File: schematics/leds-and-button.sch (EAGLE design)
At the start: 10 parts

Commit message: Reworked the boards
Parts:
- renumbered JP4 to BTN, LED_12V to 12V, LED_3.3V to 3.3V, LED_5V to 5V, LED_9V to 9V, LED_ADJV to ADJV
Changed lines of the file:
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@@
 <?xml version="1.0" encoding="utf-8"?>
 <!DOCTYPE eagle SYSTEM "eagle.dtd">
-<eagle version="6.1">
+<eagle version="7.4.0">
 <drawing>
 <settings>
@@
 </classes>
 <parts>
-<part name="LED_3.3V" library="SparkFun" deviceset="LED" device="-3MM-NO_SILK"/>
-<part name="LED_5V" library="SparkFun" deviceset="LED" device="-3MM-NO_SILK"/>
-<part name="LED_9V" library="SparkFun" deviceset="LED" device="-3MM-NO_SILK"/>
-<part name="LED_12V" library="SparkFun" deviceset="LED" device="-3MM-NO_SILK"/>
-<part name="LED_ADJV" library="SparkFun" deviceset="LED" device="-3MM-NO_SILK"/>
+<part name="3.3V" library="SparkFun" deviceset="LED" device="-3MM-NO_SILK"/>
+<part name="5V" library="SparkFun" deviceset="LED" device="-3MM-NO_SILK"/>
+<part name="9V" library="SparkFun" deviceset="LED" device="-3MM-NO_SILK"/>
+<part name="12V" library="SparkFun" deviceset="LED" device="-3MM-NO_SILK"/>
+<part name="ADJV" library="SparkFun" deviceset="LED" device="-3MM-NO_SILK"/>
 <part name="JP3" library="SparkFun" deviceset="M08" device="1X08"/>
 <part name="RN1" library="resistor-net" deviceset="RNX5" device="" value="330"/>
 <part name="JP1" library="SparkFun" deviceset="STAND-OFF" device=""/>
 <part name="JP2" library="SparkFun" deviceset="STAND-OFF" device=""/>
-<part name="JP4" library="SparkFun" deviceset="M02" device="PTH"/>
+<part name="BTN" library="SparkFun" deviceset="M02" device="PTH"/>
 </parts>
 <sheets>
@@
 </plain>
 <instances>
-<instance part="LED_3.3V" gate="G$1" x="10.16" y="25.4"/>
-<instance part="LED_5V" gate="G$1" x="17.78" y="25.4"/>
-<instance part="LED_9V" gate="G$1" x="25.4" y="25.4"/>
-<instance part="LED_12V" gate="G$1" x="33.02" y="25.4"/>
-<instance part="LED_ADJV" gate="G$1" x="40.64" y="25.4"/>
+<instance part="3.3V" gate="G$1" x="10.16" y="25.4"/>
+<instance part="5V" gate="G$1" x="17.78" y="25.4"/>
+<instance part="9V" gate="G$1" x="25.4" y="25.4"/>
+<instance part="12V" gate="G$1" x="33.02" y="25.4"/>
+<instance part="ADJV" gate="G$1" x="40.64" y="25.4"/>
 <instance part="JP3" gate="G$1" x="22.86" y="45.72" rot="R270"/>
 <instance part="RN1" gate="_" x="45.72" y="12.7" rot="R270"/>
@@
 <instance part="JP1" gate="G$1" x="2.54" y="15.24"/>
 <instance part="JP2" gate="G$1" x="2.54" y="10.16"/>
-<instance part="JP4" gate="G$1" x="7.62" y="35.56"/>
+<instance part="BTN" gate="G$1" x="7.62" y="35.56"/>
 </instances>
 <busses>
@@
 <wire x1="20.32" y1="40.64" x2="20.32" y2="30.48" width="0.1524" layer="91"/>
 <wire x1="20.32" y1="30.48" x2="10.16" y2="30.48" width="0.1524" layer="91"/>
-<pinref part="LED_3.3V" gate="G$1" pin="A"/>
+<pinref part="3.3V" gate="G$1" pin="A"/>
 </segment>
 </net>
@@
 <wire x1="22.86" y1="40.64" x2="22.86" y2="27.94" width="0.1524" layer="91"/>
 <wire x1="22.86" y1="27.94" x2="17.78" y2="27.94" width="0.1524" layer="91"/>
-<pinref part="LED_5V" gate="G$1" pin="A"/>
+<pinref part="5V" gate="G$1" pin="A"/>
 </segment>
 </net>
@@
 <pinref part="JP3" gate="G$1" pin="5"/>
 <wire x1="25.4" y1="40.64" x2="25.4" y2="27.94" width="0.1524" layer="91"/>
-<pinref part="LED_9V" gate="G$1" pin="A"/>
+<pinref part="9V" gate="G$1" pin="A"/>
 </segment>
 </net>
@@
 <wire x1="27.94" y1="40.64" x2="27.94" y2="27.94" width="0.1524" layer="91"/>
 <wire x1="27.94" y1="27.94" x2="33.02" y2="27.94" width="0.1524" layer="91"/>
-<pinref part="LED_12V" gate="G$1" pin="A"/>
+<pinref part="12V" gate="G$1" pin="A"/>
 </segment>
 </net>
@@
 <wire x1="30.48" y1="40.64" x2="30.48" y2="30.48" width="0.1524" layer="91"/>
 <wire x1="30.48" y1="30.48" x2="40.64" y2="30.48" width="0.1524" layer="91"/>
-<pinref part="LED_ADJV" gate="G$1" pin="A"/>
+<pinref part="ADJV" gate="G$1" pin="A"/>
 </segment>
 </net>
@@
 <net name="N$2" class="0">
 <segment>
-<pinref part="LED_3.3V" gate="G$1" pin="C"/>
+<pinref part="3.3V" gate="G$1" pin="C"/>
 <pinref part="RN1" gate="-5" pin="1"/>
 <wire x1="10.16" y1="20.32" x2="10.16" y2="17.78" width="0.1524" layer="91"/>
@@
 <net name="N$3" class="0">
 <segment>
-<pinref part="LED_5V" gate="G$1" pin="C"/>
+<pinref part="5V" gate="G$1" pin="C"/>
 <pinref part="RN1" gate="-4" pin="1"/>
 <wire x1="17.78" y1="20.32" x2="17.78" y2="17.78" width="0.1524" layer="91"/>
@@
 <segment>
 <pinref part="RN1" gate="-3" pin="1"/>
-<pinref part="LED_9V" gate="G$1" pin="C"/>
+<pinref part="9V" gate="G$1" pin="C"/>
 <wire x1="25.4" y1="17.78" x2="25.4" y2="20.32" width="0.1524" layer="91"/>
 </segment>
@@
 <segment>
 <pinref part="RN1" gate="-2" pin="1"/>
-<pinref part="LED_12V" gate="G$1" pin="C"/>
+<pinref part="12V" gate="G$1" pin="C"/>
 <wire x1="33.02" y1="17.78" x2="33.02" y2="20.32" width="0.1524" layer="91"/>
 </segment>
@@
 <segment>
 <pinref part="RN1" gate="-1" pin="1"/>
-<pinref part="LED_ADJV" gate="G$1" pin="C"/>
+<pinref part="ADJV" gate="G$1" pin="C"/>
 <wire x1="40.64" y1="17.78" x2="40.64" y2="20.32" width="0.1524" layer="91"/>
 </segment>
@@
 <segment>
 <pinref part="JP3" gate="G$1" pin="1"/>
-<pinref part="JP4" gate="G$1" pin="2"/>
+<pinref part="BTN" gate="G$1" pin="2"/>
 <wire x1="15.24" y1="38.1" x2="15.24" y2="40.64" width="0.1524" layer="91"/>
 </segment>
@@
 <net name="N$12" class="0">
 <segment>
-<pinref part="JP4" gate="G$1" pin="1"/>
+<pinref part="BTN" gate="G$1" pin="1"/>
 <wire x1="15.24" y1="35.56" x2="17.78" y2="35.56" width="0.1524" layer="91"/>
 <wire x1="17.78" y1="35.56" x2="17.78" y2="38.1" width="0.1524" layer="91"/>

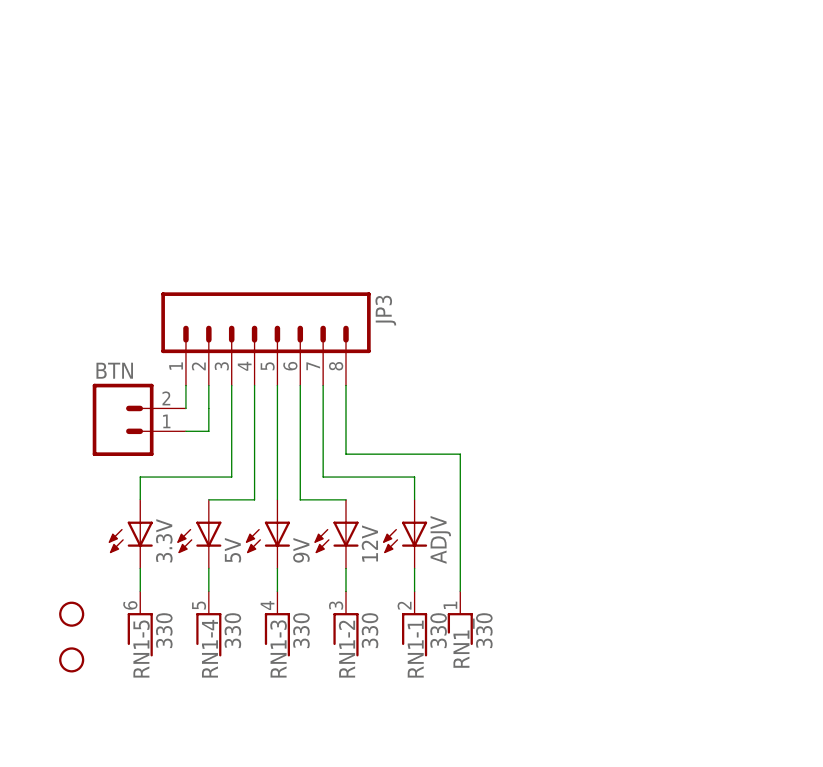
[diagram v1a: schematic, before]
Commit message: Moved the shift register to the top board since I have more room there and on the bottom board and I get to free up some pins on the jumper
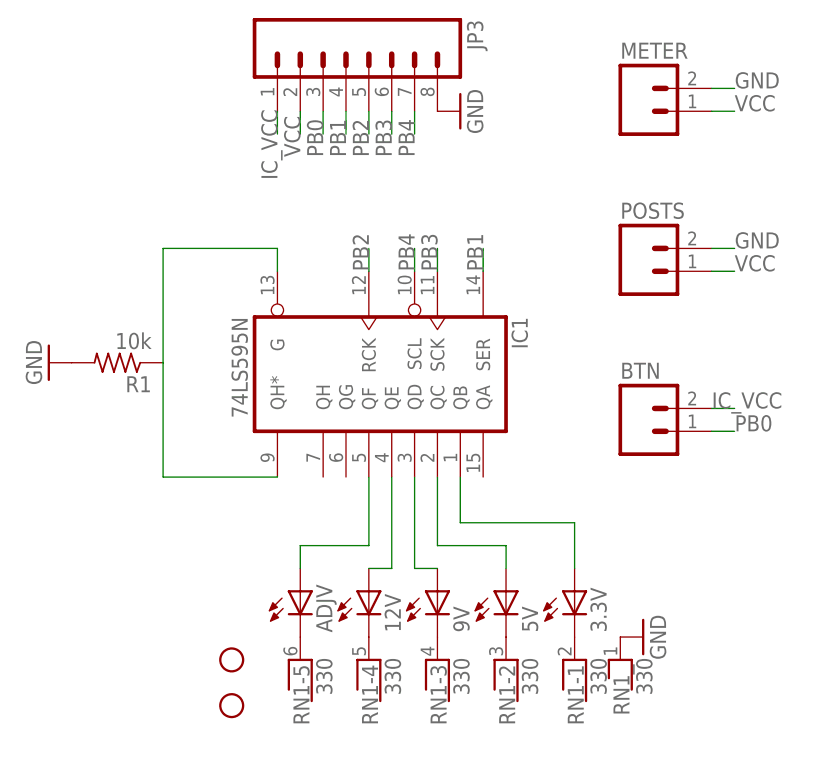
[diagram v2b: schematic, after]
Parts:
- added IC1: 74LS595N, 74xx-us:74LS595N
- added METER, POSTS: (no value), SparkFun:M02PTH
- added R1: 10k, resistor:R-US_0204/2V
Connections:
- net N$11 renamed IC_VCC
- removed net N$1: JP3.8, RN1_.1
- removed net N$12: BTN.1, JP3.2
- new net GND: JP3.8, METER.2, POSTS.2, R1.2, RN1_.1
- new net N$11: IC1A.G, IC1A.QH*, R1.1
- new net PB0: BTN.1, JP3.3
- new net PB1: IC1A.SER, JP3.4
- new net PB2: IC1A.RCK, JP3.5
- new net PB3: IC1A.SCK, JP3.6
- new net PB4: IC1A.SCL, JP3.7
- new net VCC: JP3.2, METER.1, POSTS.1
- net N$10: now also 3.3V.C; no longer ADJV.C
- net N$13: now also 3.3V.A, IC1A.QB; no longer ADJV.A, JP3.7
- net N$2: now also ADJV.C; no longer 3.3V.C
- net N$3: now also 12V.C; no longer 5V.C
- net N$4: now also ADJV.A, IC1A.QF; no longer 3.3V.A, JP3.3
- net N$5: now also 12V.A, IC1A.QE; no longer 5V.A, JP3.4
- net N$6: now also IC1A.QD; no longer JP3.5
- net N$7: now also 5V.A, IC1A.QC; no longer 12V.A, JP3.6
- net N$9: now also 5V.C; no longer 12V.C
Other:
- moved on the sheet: 12V, 3.3V, 5V, 9V, ADJV, BTN, JP3, RN1-1, RN1-2, RN1-3, RN1-4, RN1-5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

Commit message: Updated the schematics
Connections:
- net IC_VCC: now also IC1A.SCL
- net PB2: now also IC1A.SCK; no longer IC1A.RCK
- net PB3: now also IC1A.RCK; no longer IC1A.SCK
- net PB4: no longer IC1A.SCL
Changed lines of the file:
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@@
 <label x="73.66" y="38.1" size="1.778" layer="95"/>
+</segment>
+<segment>
+<pinref part="IC1" gate="A" pin="SCL"/>
+<wire x1="40.64" y1="53.34" x2="40.64" y2="55.88" width="0.1524" layer="91"/>
+<label x="40.64" y="53.34" size="1.778" layer="95" rot="R90"/>
 </segment>
 </net>
@@
 <net name="PB3" class="0">
 <segment>
-<pinref part="IC1" gate="A" pin="SCK"/>
-<wire x1="43.18" y1="53.34" x2="43.18" y2="55.88" width="0.1524" layer="91"/>
-<label x="43.18" y="53.34" size="1.778" layer="95" rot="R90"/>
-</segment>
-<segment>
 <pinref part="JP3" gate="G$1" pin="6"/>
 <wire x1="38.1" y1="71.12" x2="38.1" y2="68.58" width="0.1524" layer="91"/>
 <label x="38.1" y="66.04" size="1.778" layer="95" rot="R90"/>
 </segment>
+<segment>
+<pinref part="IC1" gate="A" pin="RCK"/>
+<wire x1="35.56" y1="53.34" x2="35.56" y2="55.88" width="0.1524" layer="91"/>
+<label x="35.56" y="53.34" size="1.778" layer="95" rot="R90"/>
+</segment>
 </net>
 <net name="PB4" class="0">
-<segment>
-<pinref part="IC1" gate="A" pin="SCL"/>
-<wire x1="40.64" y1="53.34" x2="40.64" y2="55.88" width="0.1524" layer="91"/>
-<label x="40.64" y="53.34" size="1.778" layer="95" rot="R90"/>
-</segment>
 <segment>
 <pinref part="JP3" gate="G$1" pin="7"/>
@@
 <net name="PB2" class="0">
 <segment>
-<pinref part="IC1" gate="A" pin="RCK"/>
-<wire x1="35.56" y1="53.34" x2="35.56" y2="55.88" width="0.1524" layer="91"/>
-<label x="35.56" y="53.34" size="1.778" layer="95" rot="R90"/>
-</segment>
-<segment>
 <pinref part="JP3" gate="G$1" pin="5"/>
 <wire x1="35.56" y1="71.12" x2="35.56" y2="68.58" width="0.1524" layer="91"/>
 <label x="35.56" y="66.04" size="1.778" layer="95" rot="R90"/>
 </segment>
+<segment>
+<pinref part="IC1" gate="A" pin="SCK"/>
+<wire x1="43.18" y1="53.34" x2="43.18" y2="55.88" width="0.1524" layer="91"/>
+<label x="43.18" y="53.34" size="1.778" layer="95" rot="R90"/>
+</segment>
 </net>

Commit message: Played around with the board for the leds
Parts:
- removed JP1: STAND-OFF, SparkFun:STAND-OFF
- 12V, 3.3V, 5V, 9V, ADJV: device SparkFun:LED-3MM-NO_SILK -> SparkFun-LED:LED3MM
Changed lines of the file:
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@@
 <layer number="54" name="bGND_GNDA" color="1" fill="9" visible="no" active="no"/>
 <layer number="56" name="wert" color="7" fill="1" visible="no" active="no"/>
+<layer number="57" name="tCAD" color="7" fill="1" visible="no" active="no"/>
+<layer number="59" name="tCarbon" color="7" fill="1" visible="no" active="no"/>
+<layer number="60" name="bCarbon" color="7" fill="1" visible="no" active="no"/>
+<layer number="90" name="Modules" color="5" fill="1" visible="no" active="no"/>
 <layer number="91" name="Nets" color="2" fill="1" visible="yes" active="yes"/>
 <layer number="92" name="Busses" color="1" fill="1" visible="yes" active="yes"/>
@@
 <layer number="111" name="LPC17xx" color="7" fill="1" visible="yes" active="yes"/>
 <layer number="112" name="tSilk" color="7" fill="1" visible="yes" active="yes"/>
+<layer number="113" name="IDFDebug" color="4" fill="1" visible="yes" active="yes"/>
 <layer number="116" name="Patch_BOT" color="9" fill="4" visible="yes" active="yes"/>
+<layer number="118" name="Rect_Pads" color="7" fill="1" visible="yes" active="yes"/>
 <layer number="121" name="_tsilk" color="7" fill="1" visible="no" active="yes"/>
 <layer number="122" name="_bsilk" color="7" fill="1" visible="no" active="yes"/>
@@
 <layer number="127" name="_tValues" color="7" fill="1" visible="yes" active="yes"/>
 <layer number="128" name="_bValues" color="7" fill="1" visible="yes" active="yes"/>
+<layer number="129" name="Mask" color="7" fill="1" visible="yes" active="yes"/>
 <layer number="131" name="tAdjust" color="7" fill="1" visible="no" active="yes"/>
 <layer number="132" name="bAdjust" color="7" fill="1" visible="no" active="yes"/>
 <layer number="144" name="Drill_legend" color="7" fill="1" visible="no" active="yes"/>
+<layer number="150" name="Notes" color="7" fill="1" visible="yes" active="yes"/>
 <layer number="151" name="HeatSink" color="7" fill="1" visible="yes" active="yes"/>
 <layer number="152" name="_bDocu" color="7" fill="1" visible="yes" active="yes"/>
+<layer number="153" name="FabDoc1" color="7" fill="1" visible="yes" active="yes"/>
+<layer number="154" name="FabDoc2" color="7" fill="1" visible="yes" active="yes"/>
+<layer number="155" name="FabDoc3" color="7" fill="1" visible="yes" active="yes"/>
 <layer number="199" name="Contour" color="7" fill="1" visible="yes" active="yes"/>
 <layer number="200" name="200bmp" color="1" fill="10" visible="no" active="no"/>
@@
 <layer number="223" name="223bmp" color="24" fill="1" visible="no" active="no"/>
 <layer number="224" name="224bmp" color="25" fill="1" visible="no" active="no"/>
+<layer number="225" name="225bmp" color="7" fill="1" visible="yes" active="yes"/>
+<layer number="226" name="226bmp" color="7" fill="1" visible="yes" active="yes"/>
+<layer number="227" name="227bmp" color="7" fill="1" visible="yes" active="yes"/>
+<layer number="228" name="228bmp" color="7" fill="1" visible="yes" active="yes"/>
+<layer number="229" name="229bmp" color="7" fill="1" visible="yes" active="yes"/>
+<layer number="230" name="230bmp" color="7" fill="1" visible="yes" active="yes"/>
+<layer number="231" name="231bmp" color="7" fill="1" visible="yes" active="yes"/>
 <layer number="248" name="Housing" color="7" fill="1" visible="yes" active="yes"/>
 <layer number="249" name="Edge" color="7" fill="1" visible="yes" active="yes"/>
@@
 <layer number="251" name="SMDround" color="7" fill="1" visible="no" active="no"/>
 <layer number="254" name="cooling" color="7" fill="1" visible="yes" active="yes"/>
+<layer number="255" name="routoute" color="7" fill="1" visible="yes" active="yes"/>
 </layers>
 <schematic>
@@
 </classes>
 <parts>
-<part name="ADJV" library="SparkFun" deviceset="LED" device="-3MM-NO_SILK"/>
-<part name="12V" library="SparkFun" deviceset="LED" device="-3MM-NO_SILK"/>
-<part name="9V" library="SparkFun" deviceset="LED" device="-3MM-NO_SILK"/>
-<part name="5V" library="SparkFun" deviceset="LED" device="-3MM-NO_SILK"/>
-<part name="3.3V" library="SparkFun" deviceset="LED" device="-3MM-NO_SILK"/>
 <part name="JP3" library="SparkFun" deviceset="M08" device="1X08"/>
 <part name="RN1" library="resistor-net" deviceset="RNX5" device="" value="330"/>
-<part name="JP1" library="SparkFun" deviceset="STAND-OFF" device=""/>
 <part name="JP2" library="SparkFun" deviceset="STAND-OFF" device=""/>
 <part name="BTN" library="SparkFun" deviceset="M02" device="PTH"/>
@@
 <part name="POSTS" library="SparkFun" deviceset="M02" device="PTH"/>
 <part name="METER" library="SparkFun" deviceset="M02" device="PTH"/>
+<part name="ADJV" library="SparkFun-LED" deviceset="LED" device="3MM"/>
+<part name="12V" library="SparkFun-LED" deviceset="LED" device="3MM"/>
+<part name="9V" library="SparkFun-LED" deviceset="LED" device="3MM"/>
+<part name="5V" library="SparkFun-LED" deviceset="LED" device="3MM"/>
+<part name="3.3V" library="SparkFun-LED" deviceset="LED" device="3MM"/>
 </parts>
 <sheets>
@@
 </plain>
 <instances>
-<instance part="ADJV" gate="G$1" x="27.94" y="17.78"/>
-<instance part="12V" gate="G$1" x="35.56" y="17.78"/>
-<instance part="9V" gate="G$1" x="43.18" y="17.78"/>
-<instance part="5V" gate="G$1" x="50.8" y="17.78"/>
-<instance part="3.3V" gate="G$1" x="58.42" y="17.78"/>
 <instance part="JP3" gate="G$1" x="33.02" y="76.2" rot="R270"/>
 <instance part="RN1" gate="_" x="63.5" y="7.62" rot="R270"/>
@@
 <instance part="RN1" gate="-4" x="35.56" y="10.16" rot="R270"/>
 <instance part="RN1" gate="-5" x="27.94" y="10.16" rot="R270"/>
-<instance part="JP1" gate="G$1" x="20.32" y="10.16"/>
 <instance part="JP2" gate="G$1" x="20.32" y="5.08"/>
 <instance part="BTN" gate="G$1" x="66.04" y="35.56"/>
@@
 <instance part="POSTS" gate="G$1" x="66.04" y="53.34"/>
 <instance part="METER" gate="G$1" x="66.04" y="71.12"/>
+<instance part="ADJV" gate="G$1" x="27.94" y="17.78"/>
+<instance part="12V" gate="G$1" x="35.56" y="17.78"/>
+<instance part="9V" gate="G$1" x="43.18" y="17.78"/>
+<instance part="5V" gate="G$1" x="50.8" y="17.78"/>
+<instance part="3.3V" gate="G$1" x="58.42" y="17.78"/>
 </instances>
 <busses>
@@
 <net name="N$4" class="0">
 <segment>
-<pinref part="ADJV" gate="G$1" pin="A"/>
 <wire x1="27.94" y1="22.86" x2="27.94" y2="20.32" width="0.1524" layer="91"/>
 <wire x1="35.56" y1="22.86" x2="27.94" y2="22.86" width="0.1524" layer="91"/>
 <pinref part="IC1" gate="A" pin="QF"/>
 <wire x1="35.56" y1="22.86" x2="35.56" y2="30.48" width="0.1524" layer="91"/>
+<pinref part="ADJV" gate="G$1" pin="A"/>
 </segment>
 </net>
 <net name="N$5" class="0">
 <segment>
-<pinref part="12V" gate="G$1" pin="A"/>
 <wire x1="35.56" y1="20.32" x2="38.1" y2="20.32" width="0.1524" layer="91"/>
 <pinref part="IC1" gate="A" pin="QE"/>
 <wire x1="38.1" y1="20.32" x2="38.1" y2="30.48" width="0.1524" layer="91"/>
+<pinref part="12V" gate="G$1" pin="A"/>
 </segment>
 </net>
@@
 <segment>
 <wire x1="50.8" y1="22.86" x2="50.8" y2="20.32" width="0.1524" layer="91"/>
-<pinref part="5V" gate="G$1" pin="A"/>
 <wire x1="50.8" y1="22.86" x2="43.18" y2="22.86" width="0.1524" layer="91"/>
 <pinref part="IC1" gate="A" pin="QC"/>
 <wire x1="43.18" y1="22.86" x2="43.18" y2="30.48" width="0.1524" layer="91"/>
+<pinref part="5V" gate="G$1" pin="A"/>
 </segment>
 </net>
@@
 <segment>
 <wire x1="58.42" y1="25.4" x2="58.42" y2="20.32" width="0.1524" layer="91"/>
-<pinref part="3.3V" gate="G$1" pin="A"/>
 <wire x1="58.42" y1="25.4" x2="45.72" y2="25.4" width="0.1524" layer="91"/>
 <pinref part="IC1" gate="A" pin="QB"/>
 <wire x1="45.72" y1="30.48" x2="45.72" y2="25.4" width="0.1524" layer="91"/>
-</segment>
-</net>
-<net name="N$2" class="0">
-<segment>
-<pinref part="ADJV" gate="G$1" pin="C"/>
-<pinref part="RN1" gate="-5" pin="1"/>
-</segment>
-</net>
-<net name="N$3" class="0">
-<segment>
-<pinref part="12V" gate="G$1" pin="C"/>
-<pinref part="RN1" gate="-4" pin="1"/>
-</segment>
-</net>
-<net name="N$8" class="0">
-<segment>
-<pinref part="RN1" gate="-3" pin="1"/>
-<pinref part="9V" gate="G$1" pin="C"/>
-</segment>
-</net>
-<net name="N$9" class="0">
-<segment>
-<pinref part="RN1" gate="-2" pin="1"/>
-<pinref part="5V" gate="G$1" pin="C"/>
-</segment>
-</net>
-<net name="N$10" class="0">
-<segment>
-<pinref part="RN1" gate="-1" pin="1"/>
-<pinref part="3.3V" gate="G$1" pin="C"/>
+<pinref part="3.3V" gate="G$1" pin="A"/>
 </segment>
 </net>
@@
 <net name="N$6" class="0">
 <segment>
-<pinref part="9V" gate="G$1" pin="A"/>
 <wire x1="43.18" y1="20.32" x2="40.64" y2="20.32" width="0.1524" layer="91"/>
 <pinref part="IC1" gate="A" pin="QD"/>
 <wire x1="40.64" y1="20.32" x2="40.64" y2="30.48" width="0.1524" layer="91"/>
+<pinref part="9V" gate="G$1" pin="A"/>
 </segment>
 </net>
@@
 </segment>
 </net>
+<net name="N$1" class="0">
+<segment>
+<pinref part="RN1" gate="-5" pin="1"/>
+<pinref part="ADJV" gate="G$1" pin="C"/>
+</segment>
+</net>
+<net name="N$2" class="0">
+<segment>
+<pinref part="RN1" gate="-4" pin="1"/>
+<pinref part="12V" gate="G$1" pin="C"/>
+</segment>
+</net>
+<net name="N$3" class="0">
+<segment>
+<pinref part="RN1" gate="-3" pin="1"/>
+<pinref part="9V" gate="G$1" pin="C"/>
+</segment>
+</net>
+<net name="N$8" class="0">
+<segment>
+<pinref part="RN1" gate="-2" pin="1"/>
+<pinref part="5V" gate="G$1" pin="C"/>
+</segment>
+</net>
+<net name="N$9" class="0">
+<segment>
+<pinref part="RN1" gate="-1" pin="1"/>
+<pinref part="3.3V" gate="G$1" pin="C"/>
+</segment>
+</net>
